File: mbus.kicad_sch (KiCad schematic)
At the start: 36 parts, among them J1 USB_C_Receptacle_USB2.0, J2 MBUS, Q1 BC817, Q2 BC817, Q3 BC807, U1 AP3015, U2 USBLC6-2SC6, U3 CH340E

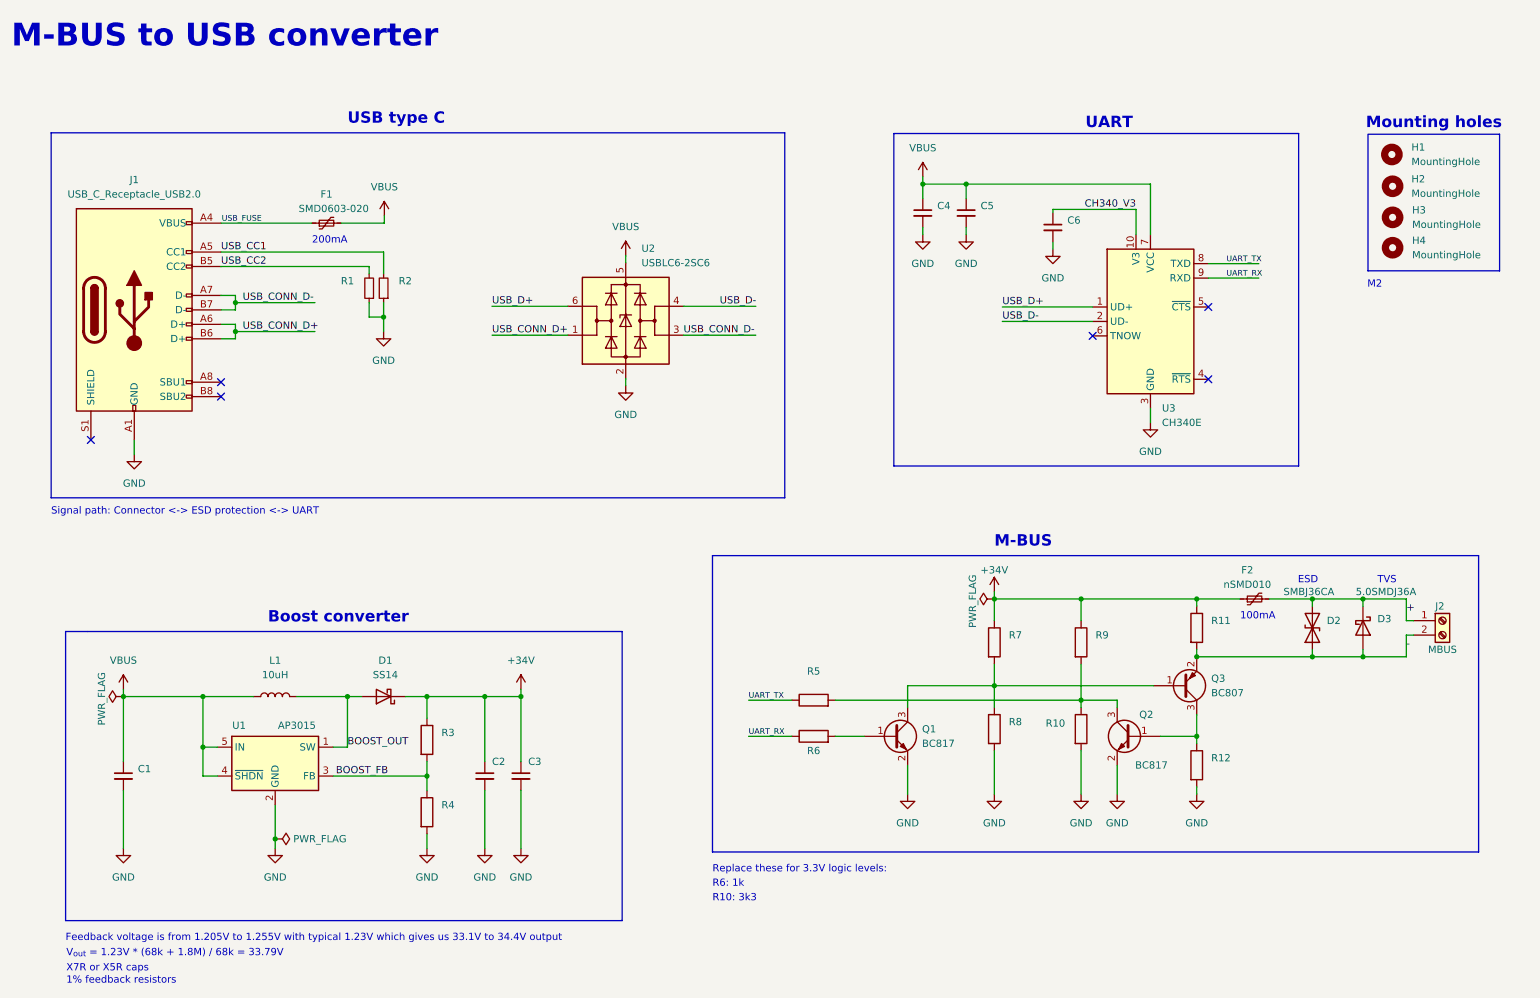
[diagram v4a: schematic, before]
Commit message: rev 0.2 - swapped RX/TX pins
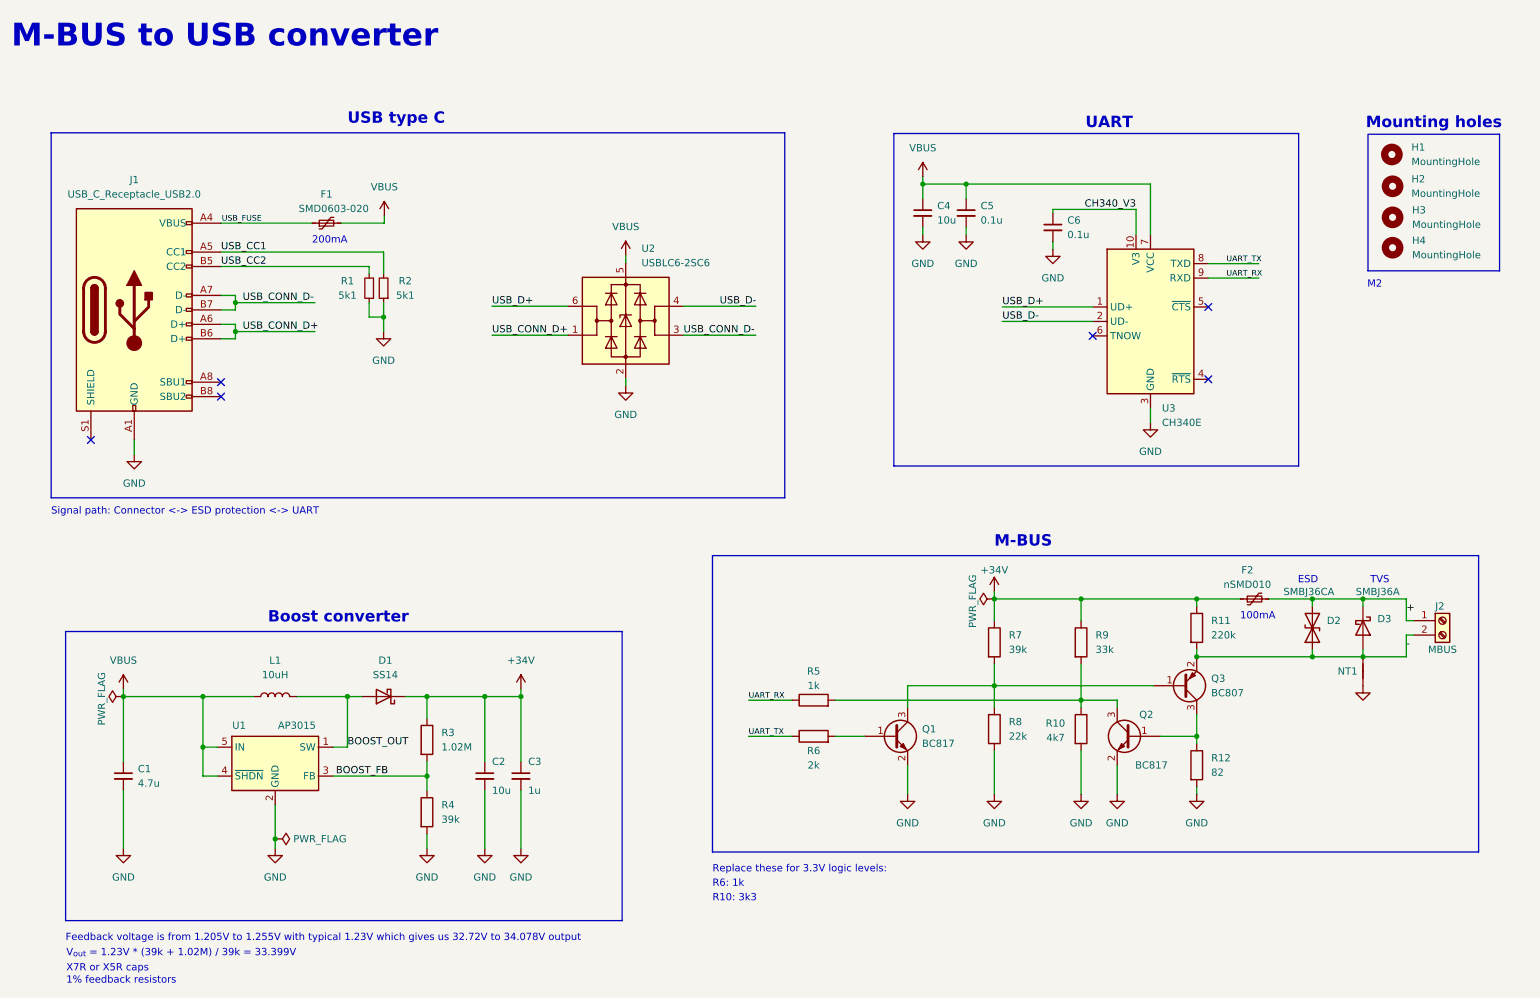
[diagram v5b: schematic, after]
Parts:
- added NT1: (no value), symbol Device:NetTie_2
- C1: value (none) -> 4.7u; footprint (none) -> Capacitor_SMD:C_0603_1608Metric
- C2: value (none) -> 10u; footprint (none) -> Capacitor_SMD:C_0603_1608Metric
- C3: value (none) -> 1u; footprint (none) -> Capacitor_SMD:C_0603_1608Metric
- C4: value (none) -> 10u; footprint (none) -> Capacitor_SMD:C_0603_1608Metric; LCSC Part C15525 -> C109455
- C5, C6: value (none) -> 0.1u; footprint (none) -> Capacitor_SMD:C_0603_1608Metric; LCSC Part C169292 -> C14663
- D3: value 5.0SMDJ36A -> SMBJ36A; footprint Diode_SMD:D_SMC -> Diode_SMD:D_SMB; LCSC Part C522690 -> C84731
- R1, R2: value (none) -> 5k1; footprint (none) -> Resistor_SMD:R_0603_1608Metric; LCSC Part C203181 -> C105580
- R10: value (none) -> 4k7; footprint (none) -> Resistor_SMD:R_0603_1608Metric
- R11: value (none) -> 220k; footprint (none) -> Resistor_SMD:R_0603_1608Metric
- R12: value (none) -> 82; footprint (none) -> Resistor_SMD:R_0603_1608Metric
- R3: value (none) -> 1.02M; footprint (none) -> Resistor_SMD:R_0603_1608Metric; LCSC Part C177951 -> C227665
- R4: value (none) -> 39k; footprint (none) -> Resistor_SMD:R_0603_1608Metric; LCSC Part C667733 -> C118370
- R5: value (none) -> 1k; footprint (none) -> Resistor_SMD:R_0603_1608Metric
- R6: value (none) -> 2k; footprint (none) -> Resistor_SMD:R_0603_1608Metric
- R7: value (none) -> 39k; footprint (none) -> Resistor_SMD:R_0603_1608Metric
- R8: value (none) -> 22k; footprint (none) -> Resistor_SMD:R_0603_1608Metric
- R9: value (none) -> 33k; footprint (none) -> Resistor_SMD:R_0603_1608Metric
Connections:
- net -: now also NT1.2
- net GND: now also NT1.1
- net UART_RX: now also R5.1; no longer R6.1
- net UART_TX: now also R6.1; no longer R5.1
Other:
- note added: "Feedback voltage is from 1.205V to 1.255V with typical 1.23V which gives us 32.72V to 34.078V output"
- note added: "V_{out} = 1.23V * (39k + 1.02M) / 39k = 33.399V"
- note removed: "Feedback voltage is from 1.205V to 1.255V with typical 1.23V which gives us 33.1V to 34.4V output"
- note removed: "V_{out} = 1.23V * (68k + 1.8M) / 68k = 33.79V"

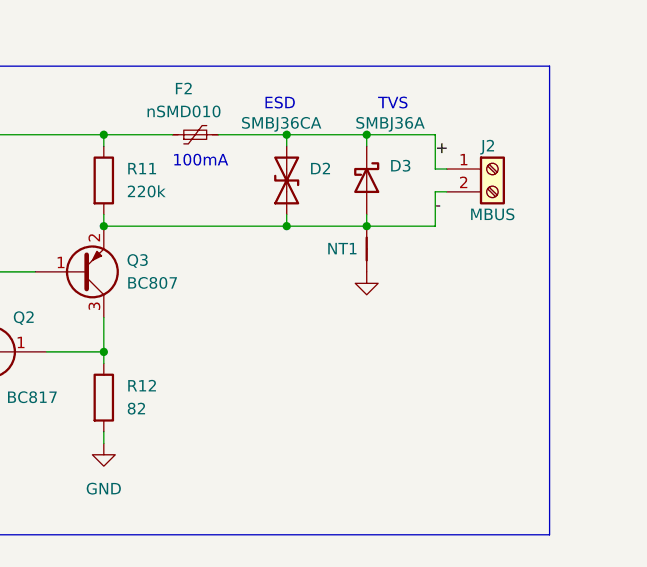
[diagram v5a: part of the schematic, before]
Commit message: Changes to enclosure, added TVS nettie
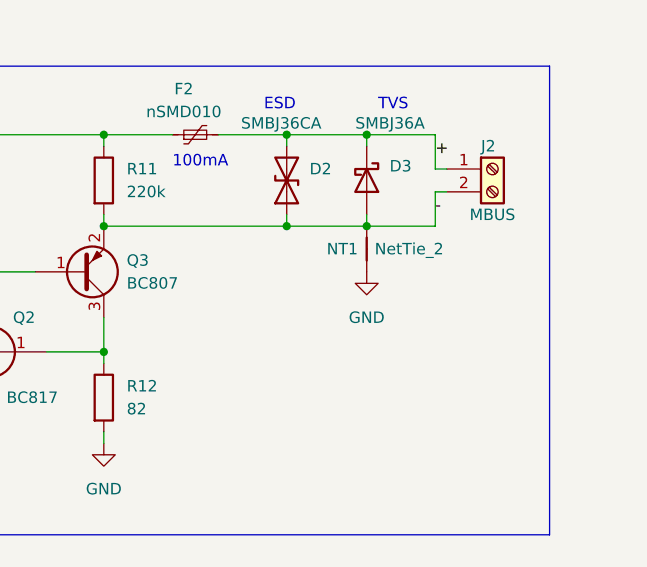
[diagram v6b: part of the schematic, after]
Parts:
- NT1: value (none) -> NetTie_2; footprint (none) -> NetTie:NetTie-2_SMD_Pad0.5mm
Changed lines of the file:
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@@
       (effects (font (size 1.27 1.27)) (justify right))
     )
-    (property "Value" "" (id 1) (at 252.349 129.54 90)
+    (property "Value" "NetTie_2" (id 1) (at 252.349 129.54 90)
       (effects (font (size 1.27 1.27)) (justify right))
     )
-    (property "Footprint" "" (id 2) (at 251.46 129.54 0)
+    (property "Footprint" "NetTie:NetTie-2_SMD_Pad0.5mm" (id 2) (at 251.46 129.54 0)
       (effects (font (size 1.27 1.27)) hide)
     )
@@
       (effects (font (size 1.27 1.27)) hide)
     )
-    (property "Value" "" (id 1) (at 251.46 137.16 0))
+    (property "Value" "GND" (id 1) (at 251.46 137.16 0))
     (property "Footprint" "" (id 2) (at 251.46 132.08 0)
       (effects (font (size 1.27 1.27)) hide)
